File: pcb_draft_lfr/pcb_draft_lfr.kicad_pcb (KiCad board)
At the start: 2 copper layers, 42.7 x 75.7 mm, 50 parts, among them J1 Conn_01x03_Pin, J10 Conn_01x02_Pin, J2 Conn_01x03_Pin, J3 Conn_01x03_Pin, J4 Conn_01x03_Pin, J5 Conn_01x03_Pin, J6 Conn_01x02_Pin, J7 Conn_01x02_Pin, J8 Conn_01x04_Pin, J9 AVR-ISP-6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

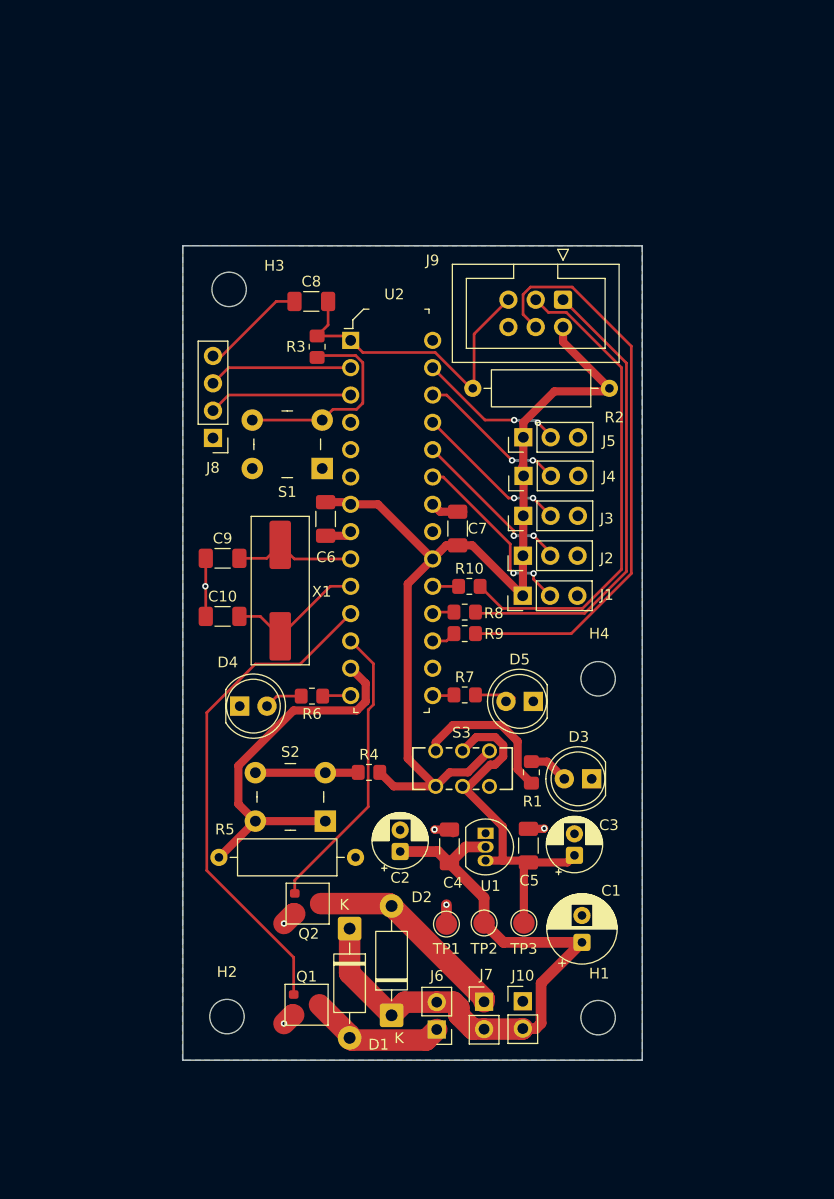
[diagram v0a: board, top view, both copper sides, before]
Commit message: Fixed the switch, and added more vias to ground for the mosfets.
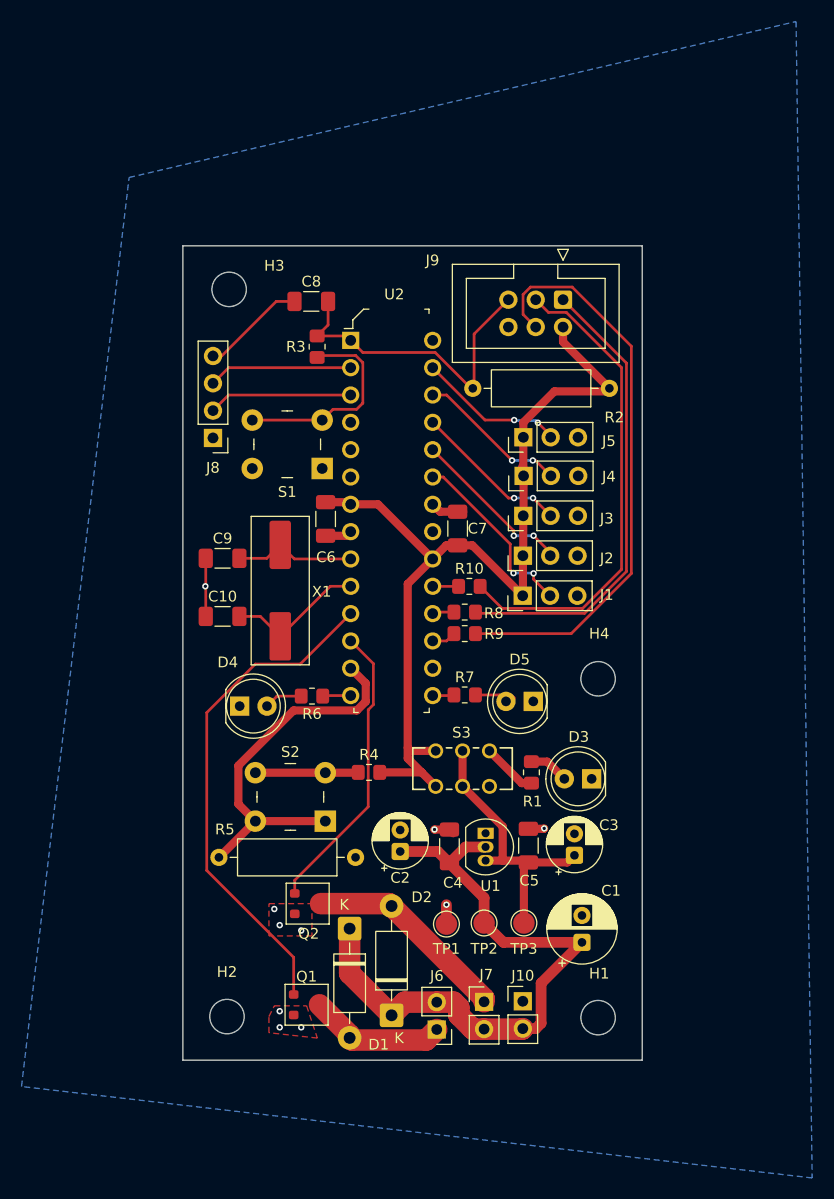
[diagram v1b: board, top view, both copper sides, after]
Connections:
- S3 pad 4: Vcc -> Net-(R1-+)
- S3 pad 6: Net-(R1-+) -> Vcc
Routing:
- net Net-(R1-+): track 14.1 -> 5.14 mm
- net Net-(U1-VO): track 33.5 -> 26.2 mm
- net Vcc: track 91.4 -> 85.9 mm
- net GND: track 19.2 -> 16.6 mm, vias 6 -> 10
- added copper zone on F.Cu, net GND
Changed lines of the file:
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@@
 			(outputformat 1)
 			(mirror no)
-			(drillshape 1)
+			(drillshape 0)
 			(scaleselection 1)
-			(outputdirectory "")
+			(outputdirectory "gerbers")
 		)
 	)
@@
 			(layers "*.Cu" "*.Mask")
 			(remove_unused_layers no)
-			(net 4 "Vcc")
+			(net 26 "Net-(R1-+)")
 			(pintype "passive")
 		)
@@
 			(layers "*.Cu" "*.Mask")
 			(remove_unused_layers no)
-			(net 26 "Net-(R1-+)")
+			(net 4 "Vcc")
 			(pintype "passive")
 		)
@@
 	)
 	(segment
-		(start 111.8 145.85)
-		(end 111.7 145.85)
-		(width 2)
-		(layer "F.Cu")
-		(net 1)
-	)
-	(segment
 		(start 116.715 101.305)
 		(end 117.1 100.92)
@@
 	)
 	(segment
-		(start 111.9 136.45)
-		(end 111.8 136.45)
-		(width 2)
-		(layer "F.Cu")
-		(net 1)
-	)
-	(segment
-		(start 111.8 136.45)
-		(end 110.9 137.35)
-		(width 2)
-		(layer "F.Cu")
-		(net 1)
-	)
-	(segment
-		(start 111.7 145.85)
-		(end 110.9 146.65)
-		(width 2)
-		(layer "F.Cu")
-		(net 1)
-	)
-	(segment
 		(start 138.25 92.17)
 		(end 138.23 92.15)
@@
 	)
 	(via
+		(at 112.5 147)
+		(size 0.6)
+		(drill 0.3)
+		(layers "F.Cu" "B.Cu")
+		(free yes)
+		(net 1)
+	)
+	(via
+		(at 110.5 145.5)
+		(size 0.6)
+		(drill 0.3)
+		(layers "F.Cu" "B.Cu")
+		(free yes)
+		(net 1)
+	)
+	(via
+		(at 112.5 138)
+		(size 0.6)
+		(drill 0.3)
+		(layers "F.Cu" "B.Cu")
+		(net 1)
+	)
+	(via
 		(at 126 135.6)
 		(size 0.6)
@@
 	)
 	(via
-		(at 110.9 137.35)
+		(at 110.5 137.5)
+		(size 0.6)
+		(drill 0.3)
+		(layers "F.Cu" "B.Cu")
+		(net 1)
+	)
+	(via
+		(at 110.5 147)
 		(size 0.6)
 		(drill 0.3)
 		(layers "F.Cu" "B.Cu")
+		(free yes)
 		(net 1)
 	)
 	(via
-		(at 110.9 146.65)
+		(at 110 136)
 		(size 0.6)
 		(drill 0.3)
@@
 	)
 	(segment
-		(start 130.07956 122.5795)
-		(end 130.529987 122.5795)
-		(width 0.76)
-		(layer "F.Cu")
-		(net 3)
-	)
-	(segment
-		(start 130.529987 122.5795)
-		(end 131.2795 121.829987)
-		(width 0.76)
-		(layer "F.Cu")
-		(net 3)
-	)
-	(segment
-		(start 127.5 124.6)
-		(end 128.05906 124.6)
-		(width 0.76)
-		(layer "F.Cu")
-		(net 3)
-	)
-	(segment
-		(start 131.2795 120.770013)
-		(end 130.529987 120.0205)
+		(start 133.2 137.3)
+		(end 133.2 132.089774)
 		(width 0.76)
 		(layer "F.Cu")
@@
 	)
 	(segment
-		(start 131.2795 121.829987)
-		(end 131.2795 120.770013)
-		(width 0.76)
-		(layer "F.Cu")
-		(net 3)
-	)
-	(segment
-		(start 128.7795 120.0205)
+		(start 127.5 124.6)
 		(end 127.5 121.3)
 		(width 0.76)
@@
 	)
 	(segment
-		(start 133.2 137.3)
-		(end 133.2 132.089774)
-		(width 0.76)
-		(layer "F.Cu")
-		(net 3)
-	)
-	(segment
-		(start 130.529987 120.0205)
-		(end 128.7795 120.0205)
-		(width 0.76)
-		(layer "F.Cu")
-		(net 3)
-	)
-	(segment
 		(start 133.2 132.089774)
 		(end 133.62 131.669774)
@@
 	)
 	(segment
-		(start 128.05906 124.6)
-		(end 130.07956 122.5795)
-		(width 0.76)
-		(layer "F.Cu")
-		(net 3)
-	)
-	(segment
 		(start 133.45 131.499774)
 		(end 133.62 131.669774)
@@
 	)
 	(segment
+		(start 122.4 105.78)
+		(end 124.72 103.46)
+		(width 0.76)
+		(layer "F.Cu")
+		(net 4)
+	)
+	(segment
 		(start 133.14 103.13)
 		(end 133.11 103.16)
@@
 	)
 	(segment
-		(start 125 124.6)
-		(end 121.1 124.6)
+		(start 136.84 83.29)
+		(end 141.15 87.6)
 		(width 0.76)
 		(layer "F.Cu")
@@
 	)
 	(segment
-		(start 122.4 122)
-		(end 122.4 105.78)
-		(width 0.76)
+		(start 122.7 121.3)
+		(end 122.4 121)
+		(width 0.2)
 		(layer "F.Cu")
 		(net 4)
 	)
 	(segment
-		(start 136.84 83.29)
-		(end 141.15 87.6)
+		(start 133.17 99.42)
+		(end 133.14 99.45)
 		(width 0.76)
 		(layer "F.Cu")
@@
 	)
 	(segment
-		(start 133.17 99.42)
-		(end 133.14 99.45)
+		(start 133.18 95.03)
+		(end 133.04 94.89)
 		(width 0.76)
 		(layer "F.Cu")
@@
 	)
 	(segment
-		(start 133.18 95.03)
-		(end 133.04 94.89)
+		(start 125 121.3)
+		(end 122.7 121.3)
 		(width 0.76)
 		(layer "F.Cu")
@@
 	)
 	(segment
-		(start 133.09 106.88)
-		(end 128.405 102.195)
+		(start 123.7 123.3)
+		(end 125 124.6)
 		(width 0.76)
 		(layer "F.Cu")
@@
 	)
 	(segment
-		(start 122.4 105.78)
-		(end 124.72 103.46)
+		(start 133.09 106.88)
+		(end 128.405 102.195)
 		(width 0.76)
 		(layer "F.Cu")
@@
 	)
 	(segment
-		(start 126.3 123.3)
-		(end 128 123.3)
-		(width 0.76)
-		(layer "F.Cu")
-		(net 4)
-	)
-	(segment
 		(start 133.15 90.77)
 		(end 136.04 87.88)
@@
 	)
 	(segment
-		(start 121.1 124.6)
-		(end 119.8 123.3)
+		(start 122.4 121)
+		(end 122.4 105.78)
 		(width 0.76)
 		(layer "F.Cu")
@@
 	)
 	(segment
-		(start 125 124.6)
-		(end 126.3 123.3)
+		(start 122.4 122)
+		(end 122.4 121)
 		(width 0.76)
 		(layer "F.Cu")
@@
 	)
 	(segment
-		(start 128 123.3)
-		(end 130 121.3)
-		(width 0.76)
-		(layer "F.Cu")
-		(net 4)
-	)
-	(segment
-		(start 125 124.6)
-		(end 122.4 122)
+		(start 123.7 123.3)
+		(end 119.8 123.3)
 		(width 0.76)
 		(layer "F.Cu")
@@
 	)
 	(segment
+		(start 122.4 122)
+		(end 123.7 123.3)
+		(width 0.76)
+		(layer "F.Cu")
+		(net 4)
+	)
+	(segment
 		(start 133.17 95.74)
 		(end 133.17 99.42)
@@
 	)
 	(segment
-		(start 131.1 118.9)
-		(end 132.619 120.419)
-		(width 0.76)
-		(layer "F.Cu")
-		(net 26)
-	)
-	(segment
-		(start 125 120.5)
-		(end 126.6 118.9)
-		(width 0.76)
-		(layer "F.Cu")
-		(net 26)
-	)
-	(segment
-		(start 126.6 118.9)
-		(end 131.1 118.9)
-		(width 0.76)
-		(layer "F.Cu")
-		(net 26)
-	)
-	(segment
-		(start 132.619 120.419)
-		(end 132.619 123.019)
-		(width 0.76)
-		(layer "F.Cu")
-		(net 26)
-	)
-	(segment
-		(start 132.619 123.019)
-		(end 133.9 124.3)
+		(start 133 124.3)
+		(end 130 121.3)
 		(width 0.76)
 		(layer "F.Cu")
@@
 	)
 	(segment
-		(start 125 121.3)
-		(end 125 120.5)
+		(start 133.9 124.3)
+		(end 133 124.3)
 		(width 0.76)
 		(layer "F.Cu")
@@
 		(net 1)
 		(net_name "GND")
-		(locked yes)
+		(layer "F.Cu")
+		(hatch edge 0.5)
+		(priority 2)
+		(connect_pads
+			(clearance 0.5)
+		)
+		(min_thickness 0.25)
+		(filled_areas_thickness no)
+		(fill yes
+			(thermal_gap 0.5)
+			(thermal_bridge_width 0.5)
+		)
+		(polygon
+			(pts
+				(xy 110 145) (xy 113 145) (xy 114 148) (xy 109.5 147.5) (xy 109.5 146)
+			)
+		)
+	)
+	(zone
+		(net 1)
+		(net_name "GND")
+		(layer "F.Cu")
+		(hatch edge 0.5)
+		(priority 1)
+		(connect_pads
+			(clearance 0.5)
+		)
+		(min_thickness 0.25)
+		(filled_areas_thickness no)
+		(fill yes
+			(thermal_gap 0.5)
+			(thermal_bridge_width 0.5)
+		)
+		(polygon
+			(pts
+				(xy 109.5 135.5) (xy 113.5 135.5) (xy 113.5 138.5) (xy 109.5 138.5)
+			)
+		)
+	)
+	(zone
+		(net 1)
+		(net_name "GND")
 		(layer "B.Cu")
 		(hatch edge 0.5)
@@
 		(polygon
 			(pts
-				(xy 101.510907 74.338329) (xy 144.189546 74.359534) (xy 144.212981 150.06389) (xy 101.464035 150.035599)
+				(xy 96.5 68) (xy 158.5 53.5) (xy 160 161) (xy 86.5 152.5)
 			)
 		)
